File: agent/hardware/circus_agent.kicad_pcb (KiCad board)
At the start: 2 copper layers, 66 parts, among them J1001 M20-9990345, J1002 M20-9990345, J61 PowerClip, J62 PowerClip, J63 PowerClip, J64 PowerClip, M71 Motor, M81 Motor, Q11 PMV65XPEA, Q12 MMBT2222LT1G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

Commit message: first stab at layout
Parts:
- moved Q41 134.6 mm to (57.9, 70.9), turned to 0 degrees
- moved C93 133.8 mm to (63.5, 63.5)
- moved M81 120.7 mm to (76.8, 89.9)
- moved U91 119.8 mm to (71.9, 77.2)
- moved C1001 119.1 mm to (79.8, 61.5)
- moved Q21 117.1 mm to (57.9, 64.3)
- moved Q86 115.6 mm to (77.5, 95.2), turned to 90 degrees
- moved U1001 105.0 mm to (79.0, 76.5)
- moved C51 103.7 mm to (69.3, 88.4)
- moved D31 102.1 mm to (74.4, 58.4)
- moved R91 97.5 mm to (60.5, 74.9)
- moved R41 95.3 mm to (61.2, 66.8), turned to 180 degrees
- moved R43 94.8 mm to (61.2, 68.1), turned to 180 degrees
- moved R44 93.4 mm to (61.7, 70.4), turned to 90 degrees
- moved R42 92.3 mm to (63.0, 70.4), turned to 90 degrees
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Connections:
- C1001 pad 2: Net-(C1001-Pad2) -> VDD
- C1002 pad 2: Net-(C1001-Pad2) -> VDD
- C51 pad 2: Net-(C51-Pad2) -> +BATT
- C92 pad 2: Net-(C92-Pad2) -> +BATT
- Q11 pad 2: Net-(Q11-Pad2) -> +BATT
- Q21 pad 2: Net-(Q21-Pad2) -> VDD
- Q41 pad 2: Net-(Q41-Pad2) -> VDD
- Q71 pad 2: Net-(Q71-Pad2) -> +BATT
- Q72 pad 2: Net-(Q71-Pad2) -> +BATT
- Q81 pad 2: Net-(Q81-Pad2) -> +BATT
- Q82 pad 2: Net-(Q81-Pad2) -> +BATT
- R1001 pad 2: Net-(R1001-Pad2) -> VDD
- R12 pad 2: Net-(Q11-Pad2) -> +BATT
- R23 pad 2: Net-(Q21-Pad2) -> VDD
- R45 pad 2: Net-(Q41-Pad2) -> VDD
- R63 pad 1: Net-(R63-Pad1) -> +BATT
- R71 pad 2: Net-(Q71-Pad2) -> +BATT
- R72 pad 2: Net-(Q71-Pad2) -> +BATT
- R81 pad 2: Net-(Q81-Pad2) -> +BATT
- R82 pad 2: Net-(Q81-Pad2) -> +BATT
- R91 pad 2: Net-(R91-Pad2) -> VDD
- R92 pad 1: Net-(C92-Pad2) -> +BATT
- U1001 pad 4: Net-(U1001-Pad4) -> VDD
- U1001 pad 6: Net-(C1001-Pad2) -> VDD
- U91 pad 1: Net-(C92-Pad2) -> +BATT
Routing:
- net GND: track 0.00 -> 88.0 mm
- net +BATT: track 0.00 -> 50.1 mm
- net LM_RVR: track 0.00 -> 20.3 mm, vias 0 -> 2
- net Net-(Q11-Pad1): track 0.00 -> 15.4 mm
- net RM_FWD: track 0.00 -> 15.0 mm, vias 0 -> 2
- net LM_FWD: track 0.00 -> 12.9 mm, vias 0 -> 2
- net RM_RVR: track 0.00 -> 11.7 mm, vias 0 -> 2
- net Net-(Q82-Pad1): track 0.00 -> 9.68 mm
- net Net-(Q73-Pad1): track 0.00 -> 9.48 mm, vias 0 -> 2
- net Net-(M81-Pad2): track 0.00 -> 8.71 mm
- net Net-(M81-Pad1): track 0.00 -> 8.67 mm
- net Net-(Q72-Pad1): track 0.00 -> 8.15 mm
- net Net-(M71-Pad2): track 0.00 -> 8.12 mm
- net Net-(M71-Pad1): track 0.00 -> 7.28 mm
- net Net-(Q71-Pad1): track 0.00 -> 5.05 mm
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
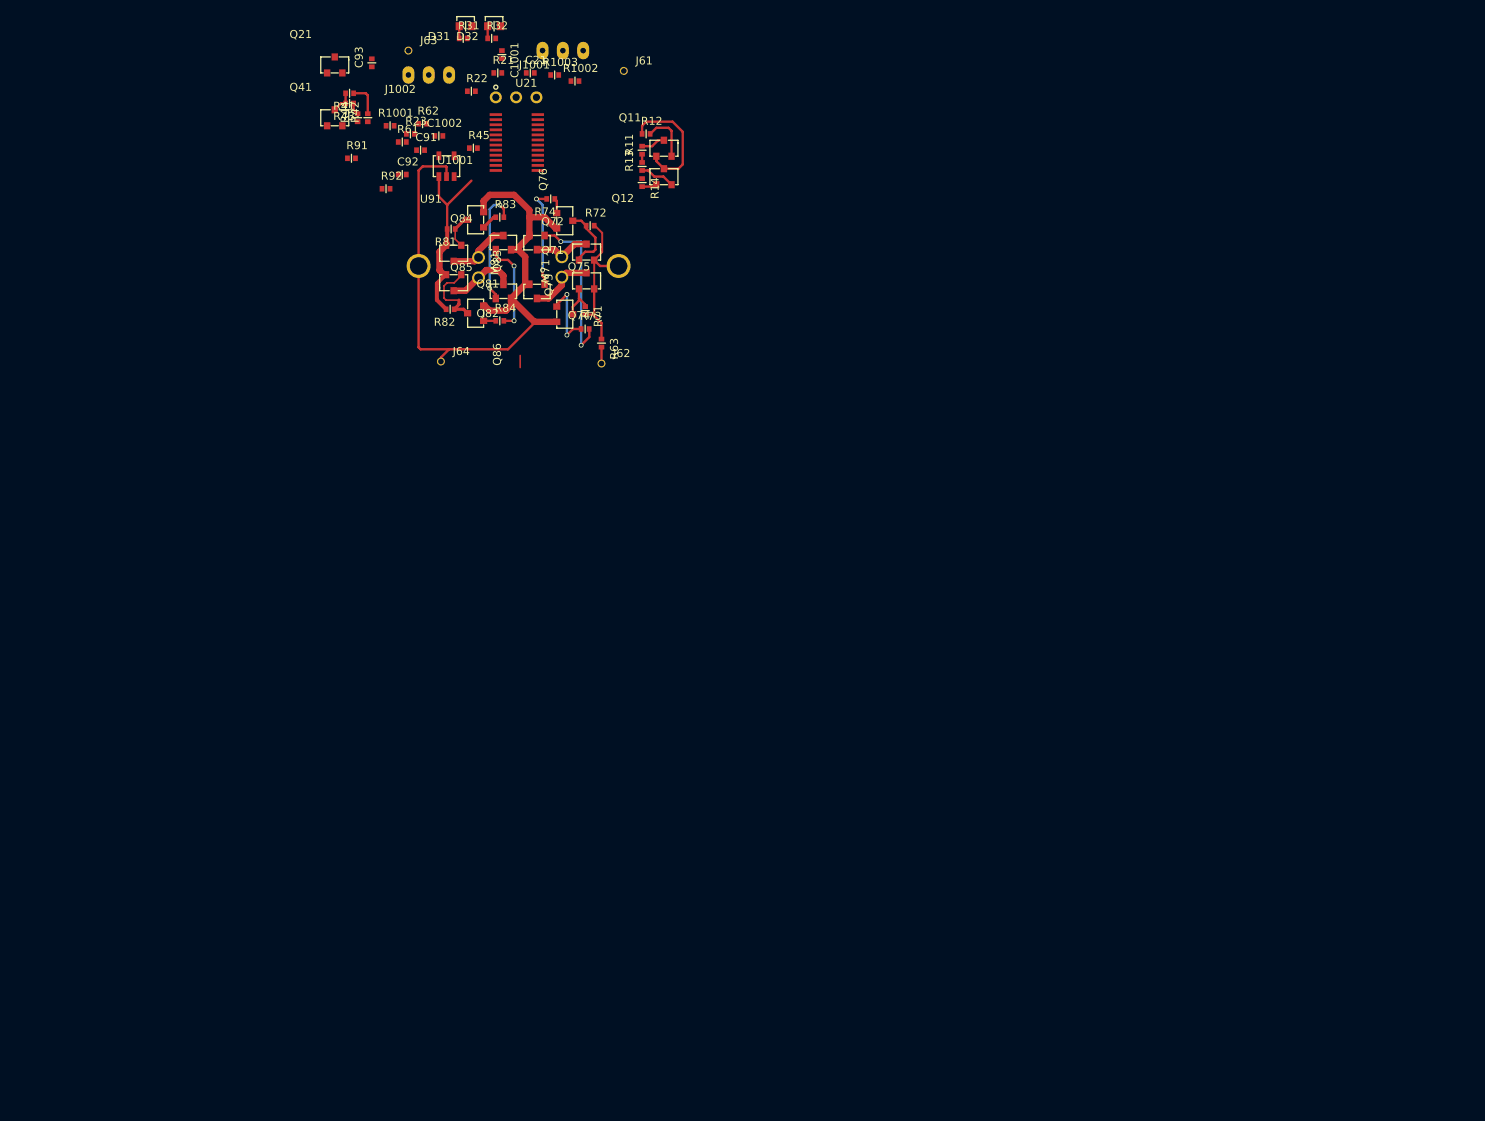
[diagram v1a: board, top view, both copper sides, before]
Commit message: First outline for PCB
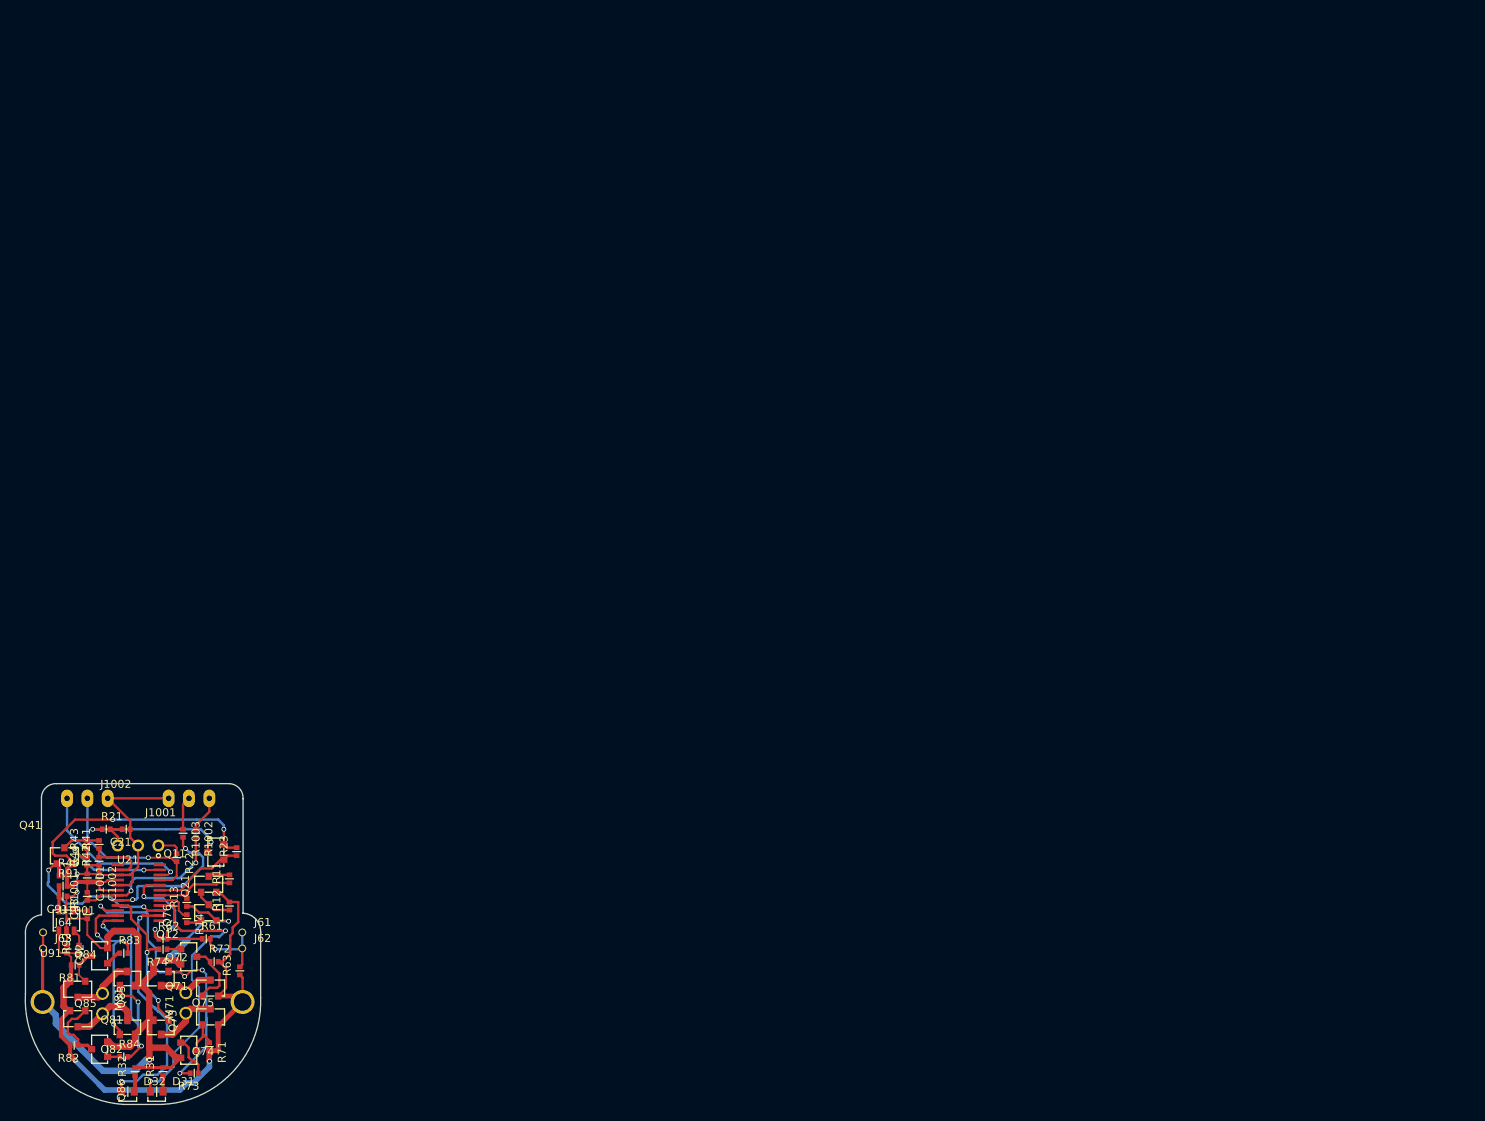
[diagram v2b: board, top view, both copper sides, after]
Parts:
- moved D32 140.3 mm to (33.8, 191.6), turned to 180 degrees
- moved D31 138.2 mm to (37.4, 191.6), turned to 180 degrees
- moved R32 136.9 mm to (33.9, 189.6), turned to 90 degrees
- moved R31 134.8 mm to (37.4, 189.6), turned to 90 degrees
- moved J63 121.2 mm to (22.4, 173.7)
- moved J61 117.8 mm to (47.3, 171.7)
- moved C1001 115.2 mm to (27.9, 164.4)
- moved C93 112.3 mm to (27.9, 170.0)
- moved R12 109.9 mm to (45.7, 168.9), turned to 90 degrees
- moved R13 108.2 mm to (40.4, 168.5)
- moved Q12 108.2 mm to (42.2, 170.2)
- moved R14 108.2 mm to (40.4, 169.5)
- moved Q11 108.2 mm to (42.2, 166.7)
- moved R62 106.9 mm to (36.9, 172.5)
- moved C21 106.7 mm to (33.3, 158.8), turned to 180 degrees
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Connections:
- U1001 pad 14: nPWR_ID -> LEDG
- U1001 pad 15: LEDG -> nPWR_ID
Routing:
- net GND: track 88.0 -> 153.6 mm, vias 0 -> 6
- net VDD: track 0.00 -> 45.7 mm, vias 0 -> 2
- net LEDR: track 0.00 -> 37.3 mm, vias 0 -> 2
- net LEDG: track 0.00 -> 31.7 mm, vias 0 -> 2
- net +BATT: track 50.1 -> 76.6 mm, vias 0 -> 2
- net LM_RVR: track 20.3 -> 42.3 mm, vias 2 -> 4
- net IR: track 0.00 -> 21.5 mm, vias 0 -> 1
- net nPWR_ID: track 0.00 -> 21.2 mm, vias 0 -> 2
- net MCU_TX: track 0.00 -> 20.6 mm, vias 0 -> 1
- net RM_RVR: track 11.7 -> 31.6 mm, vias 2 -> 3
- net Net-(R1001-Pad1): track 0.00 -> 19.6 mm, vias 0 -> 2
- net Net-(R1003-Pad2): track 0.00 -> 19.0 mm, vias 0 -> 2
- net Net-(Q21-Pad3): track 0.00 -> 18.3 mm, vias 0 -> 2
- net CHG: track 0.00 -> 16.2 mm, vias 0 -> 2
- net ID1: track 1.50 -> 17.5 mm, vias 0 -> 2
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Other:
- board outline added: 29.4 x 40.1 mm

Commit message: adjust outline
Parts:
- moved R63 0.30 mm to (47.3, 177.0)
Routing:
- net Net-(Q81-Pad1): track 4.38 -> 7.90 mm
- net Net-(Q71-Pad1): track 5.05 -> 7.34 mm
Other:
- outline, holes or cut-outs redrawn

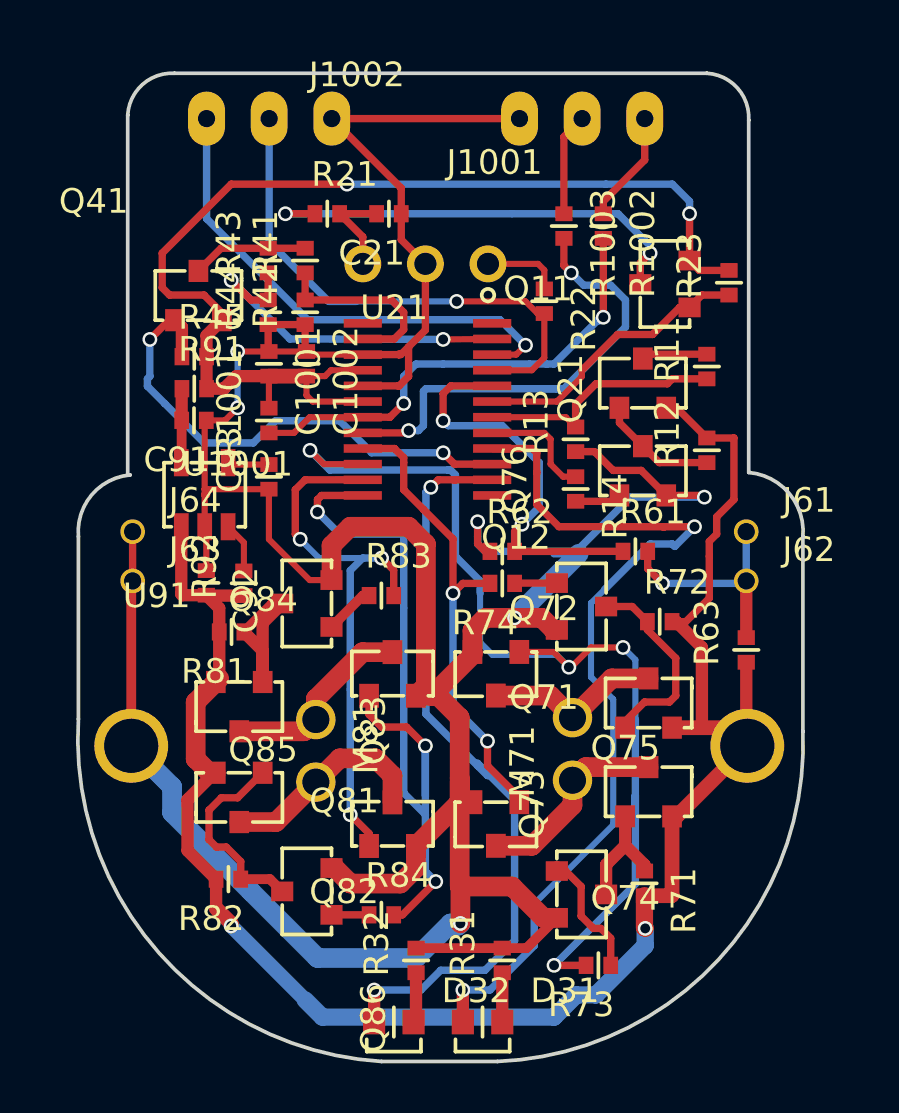
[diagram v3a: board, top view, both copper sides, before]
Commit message: Opt PCB layout and adjust drc
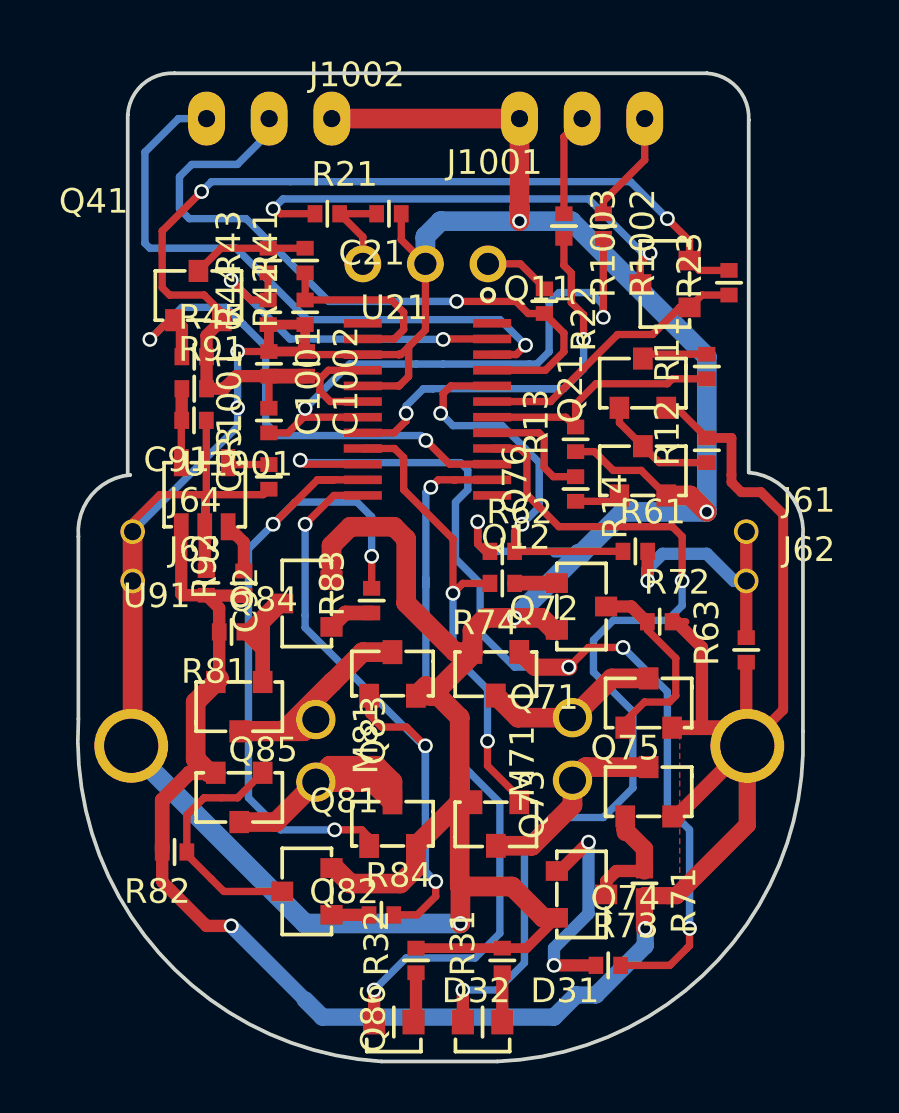
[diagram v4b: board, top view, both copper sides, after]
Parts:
- moved R82 2.45 mm to (24.6, 184.7)
- moved R83 0.71 mm to (32.1, 175.0), turned to 90 degrees
- moved R73 0.60 mm to (41.2, 189.3), turned to 0 degrees
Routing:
- net GND: track 153.6 -> 176.0 mm, vias 6 -> 7
- net +BATT: track 76.4 -> 87.7 mm
- net IR: track 21.5 -> 27.9 mm
- net RM_FWD: track 24.7 -> 30.3 mm
- net MCU_TX: track 20.6 -> 25.4 mm
- net Net-(R1001-Pad1): track 19.6 -> 23.6 mm
- net Net-(M81-Pad2): track 8.71 -> 12.7 mm
- net Net-(Q73-Pad1): track 5.63 -> 9.56 mm, vias 0 -> 2
- net Net-(Q81-Pad1): track 7.90 -> 11.8 mm
- net RM_RVR: track 31.6 -> 27.8 mm
- net Net-(M81-Pad1): track 8.67 -> 11.8 mm
- net ID1: track 17.5 -> 14.5 mm
- net Net-(R1003-Pad2): track 19.0 -> 16.8 mm
- net Net-(Q71-Pad1): track 7.34 -> 5.13 mm
- net LEDG: track 31.7 -> 29.8 mm
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- added copper zone on F.Cu, net +BATT
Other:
- net class Default: clearance 0.2 -> 0.25; trace_width 0.25 -> 0.3
- rule trace_clearance: 0.2 -> 0.25
- rule trace_min: 0.2 -> 0.3

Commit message: More layout opt and Rev A marking
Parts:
- moved R23 4.04 mm to (46.0, 158.1), turned to 180 degrees
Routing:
- net nPWR_IR: track 11.4 -> 15.6 mm
- net IR: track 27.9 -> 24.4 mm, vias 1 -> 2
- net Net-(R1001-Pad1): track 23.6 -> 21.4 mm
- net CHG: track 16.2 -> 14.3 mm
- net +BATT: track 87.7 -> 86.2 mm
- net Net-(R1003-Pad2): track 16.8 -> 18.1 mm
- net Net-(Q72-Pad1): track 8.15 -> 9.39 mm
- net GND: track 176.0 -> 174.8 mm
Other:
- board text added: "AJR"
- board text added: "Circus Rev A"

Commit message: final route opt
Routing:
- net GND: track 174.8 -> 190.9 mm
- net RM_FWD: track 30.3 -> 29.4 mm
- net VDD: track 44.8 -> 44.0 mm
- net IR: track 24.4 -> 25.1 mm
